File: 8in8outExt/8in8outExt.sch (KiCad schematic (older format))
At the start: 48 parts, among them P1 CONN_10X2, SW1 SPST, SW2 SPST, SW3 SPST, SW4 SPST, SW5 SPST, SW6 SPST, SW7 SPST, SW8 SPST, U1 ULN2803, U2 ULN2803

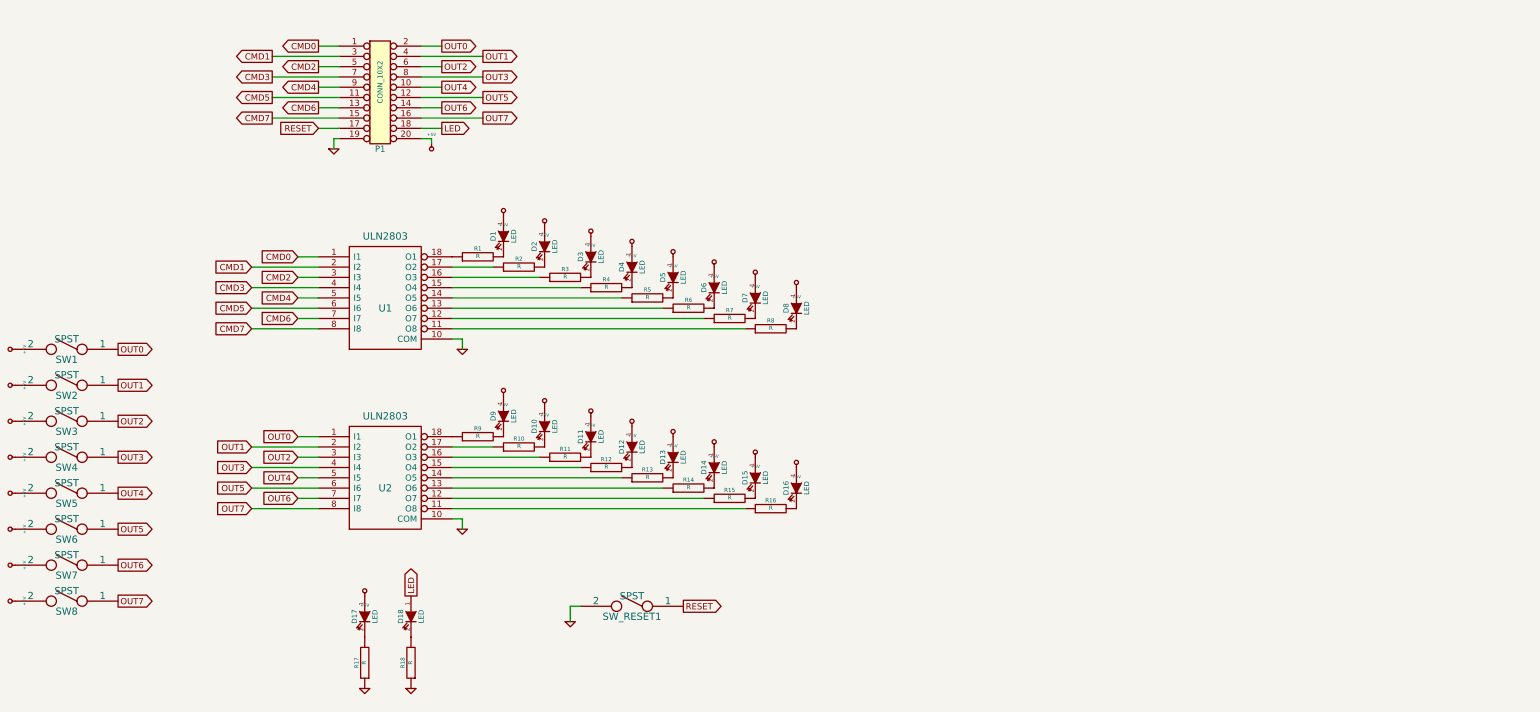
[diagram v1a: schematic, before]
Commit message: ajout resistance forcage sortie routage incomplet
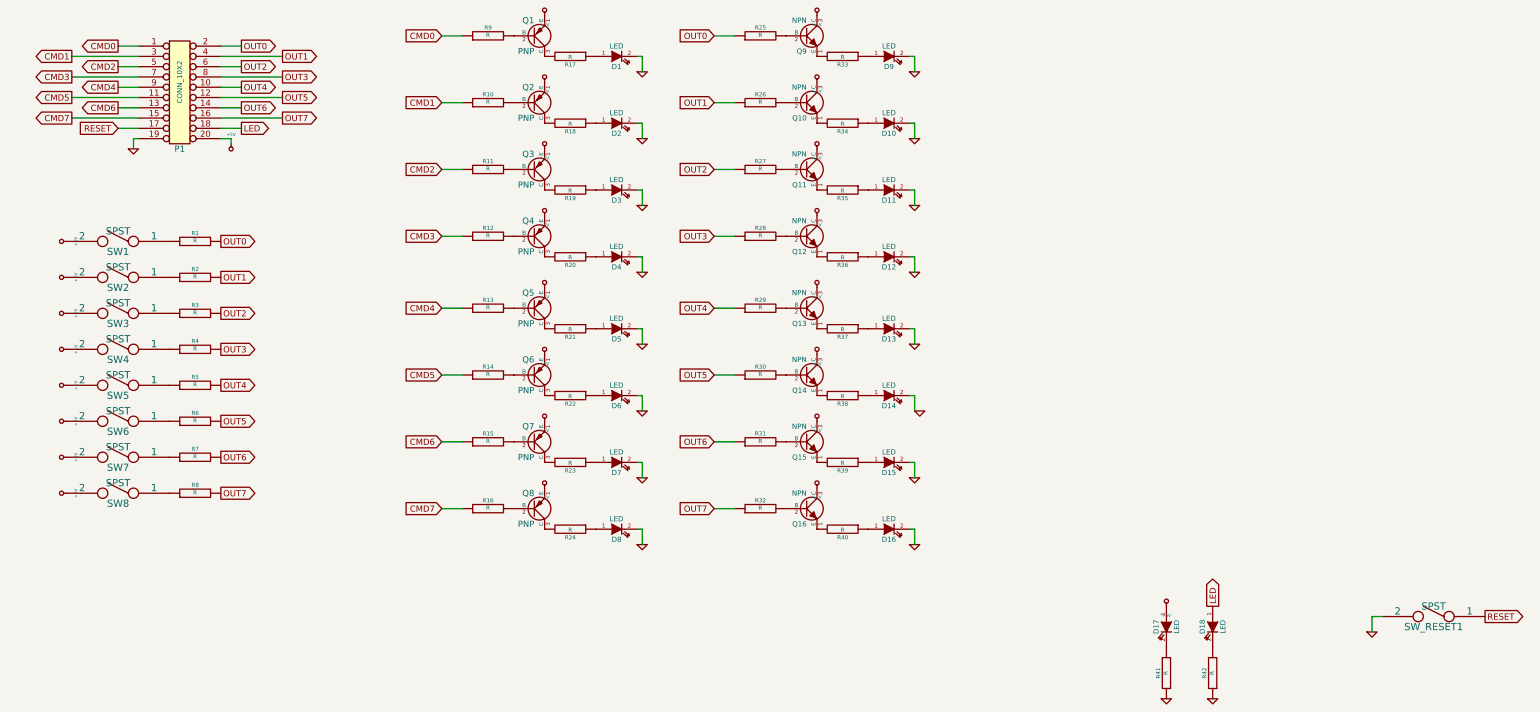
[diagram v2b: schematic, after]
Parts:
- removed U1, U2: ULN2803, ~, symbol ULN2803
- added Q1, Q2, Q3, Q4, Q5, Q6, Q7, Q8: PNP, symbol PNP
- added Q10, Q11, Q12, Q13, Q14, Q15, Q16, Q9: NPN, symbol NPN
- added R1, R25, R26, R27, R28, R29, R30, R31, R32: R, symbol R
- added R18, R19, R20, R21, R22, R23, R24, R33, R34, R35, R36, R37, R38, R39, R40: R, ~, symbol R
- R10, R11, R12, R13, R14, R15, R16, R2, R3, R4, R5, R6, R7, R8, R9: footprint ~ -> (none)
- renumbered R1 to R17, R17 to R41, R18 to R42
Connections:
- net +5V: now also Q1.1 (E), Q10.3 (C), Q11.3 (C), Q12.3 (C), Q13.3 (C), Q14.3 (C), Q15.3 (C), Q16.3 (C), Q2.1 (E), Q3.1 (E), Q4.1 (E), Q5.1 (E), Q6.1 (E), Q7.1 (E), Q8.1 (E), Q9.3 (C); no longer D1.1 (A), D10.1 (A), D11.1 (A), D12.1 (A), D13.1 (A), D14.1 (A), D15.1 (A), D16.1 (A), D2.1 (A), D3.1 (A), D4.1 (A), D5.1 (A), D6.1 (A), D7.1 (A), D8.1 (A), D9.1 (A)
- net CMD0: now also R9.1
- net CMD1: now also R10.1
- net CMD2: now also R11.1
- net CMD3: now also R12.1
- net CMD4: now also R13.1
- net CMD5: now also R14.1
- net CMD6: now also R15.1
- net CMD7: now also R16.1
- net GND: now also D1.2 (K), D10.2 (K), D11.2 (K), D12.2 (K), D13.2 (K), D15.2 (K), D16.2 (K), D2.2 (K), D3.2 (K), D4.2 (K), D5.2 (K), D6.2 (K), D7.2 (K), D8.2 (K), D9.2 (K)
- net OUT0: now also R1.2, R25.1; no longer SW1.1
- net OUT1: now also R2.2, R26.1; no longer SW2.1
- net OUT2: now also R3.2, R27.1; no longer SW3.1
- net OUT3: now also R4.2, R28.1; no longer SW4.1
- net OUT4: now also R5.2, R29.1; no longer SW5.1
- net OUT5: now also R6.2, R30.1; no longer SW6.1
- net OUT6: now also R7.2, R31.1; no longer SW7.1
- net OUT7: now also R8.2, R32.1; no longer SW8.1
- net at R8.1: now also SW8.1
- net at R7.1: now also SW7.1
- net at R6.1: now also SW6.1
- net at R5.1: now also SW5.1
- net at R4.1: now also SW4.1
- net at R3.1: now also SW3.1
- net at R2.1: now also SW2.1
- net at R17.1: now also D1.1 (A)
- net at R17.2: now also Q1.3 (C); no longer D1.2 (K)
- net at R9.2: now also Q1.2 (B); no longer D9.2 (K)
- net at R10.2: now also Q2.2 (B); no longer D10.2 (K)
- net at R11.2: now also Q3.2 (B); no longer D11.2 (K)
- net at R12.2: now also Q4.2 (B); no longer D12.2 (K)
- net at R13.2: now also Q5.2 (B); no longer D13.2 (K)
- net at R14.2: now also Q6.2 (B); no longer D14.2 (K)
- net at R15.2: now also Q7.2 (B); no longer D15.2 (K)
- net at R16.2: now also Q8.2 (B); no longer D16.2 (K)
- new net: R1.1, SW1.1
- new net: D2.1 (A), R18.1
- new net: Q2.3 (C), R18.2
- new net: D3.1 (A), R19.1
- new net: Q3.3 (C), R19.2
- new net: D4.1 (A), R20.1
- new net: Q4.3 (C), R20.2
- new net: D5.1 (A), R21.1
- new net: Q5.3 (C), R21.2
- new net: D6.1 (A), R22.1
- new net: Q6.3 (C), R22.2
- new net: D7.1 (A), R23.1
- new net: Q7.3 (C), R23.2
- new net: D8.1 (A), R24.1
- new net: Q8.3 (C), R24.2
- new net: D9.1 (A), R33.1
- new net: Q9.1 (E), R33.2
- new net: Q9.2 (B), R25.2
- new net: D10.1 (A), R34.1
- new net: Q10.1 (E), R34.2
- new net: Q10.2 (B), R26.2
- new net: D11.1 (A), R35.1
- new net: Q11.1 (E), R35.2
- new net: Q11.2 (B), R27.2
- new net: D12.1 (A), R36.1
- new net: Q12.1 (E), R36.2
- new net: Q12.2 (B), R28.2
- new net: D13.1 (A), R37.1
- new net: Q13.1 (E), R37.2
- new net: Q13.2 (B), R29.2
- new net: D14.1 (A), R38.1
- new net: Q14.1 (E), R38.2
- new net: Q14.2 (B), R30.2
- new net: D15.1 (A), R39.1
- new net: Q15.1 (E), R39.2
- new net: Q15.2 (B), R31.2
- new net: D16.1 (A), R40.1
- new net: Q16.1 (E), R40.2
- new net: Q16.2 (B), R32.2
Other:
- moved on the sheet: D1, D17, D18, P1, R17, R41, R42, SW1, SW2, SW3, SW4, SW5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
